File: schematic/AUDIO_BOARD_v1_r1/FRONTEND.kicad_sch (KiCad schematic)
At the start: 18 parts, among them J2 U.FL L in, J3 U.FL R in, U2 OPA1678, U3 OPA1678

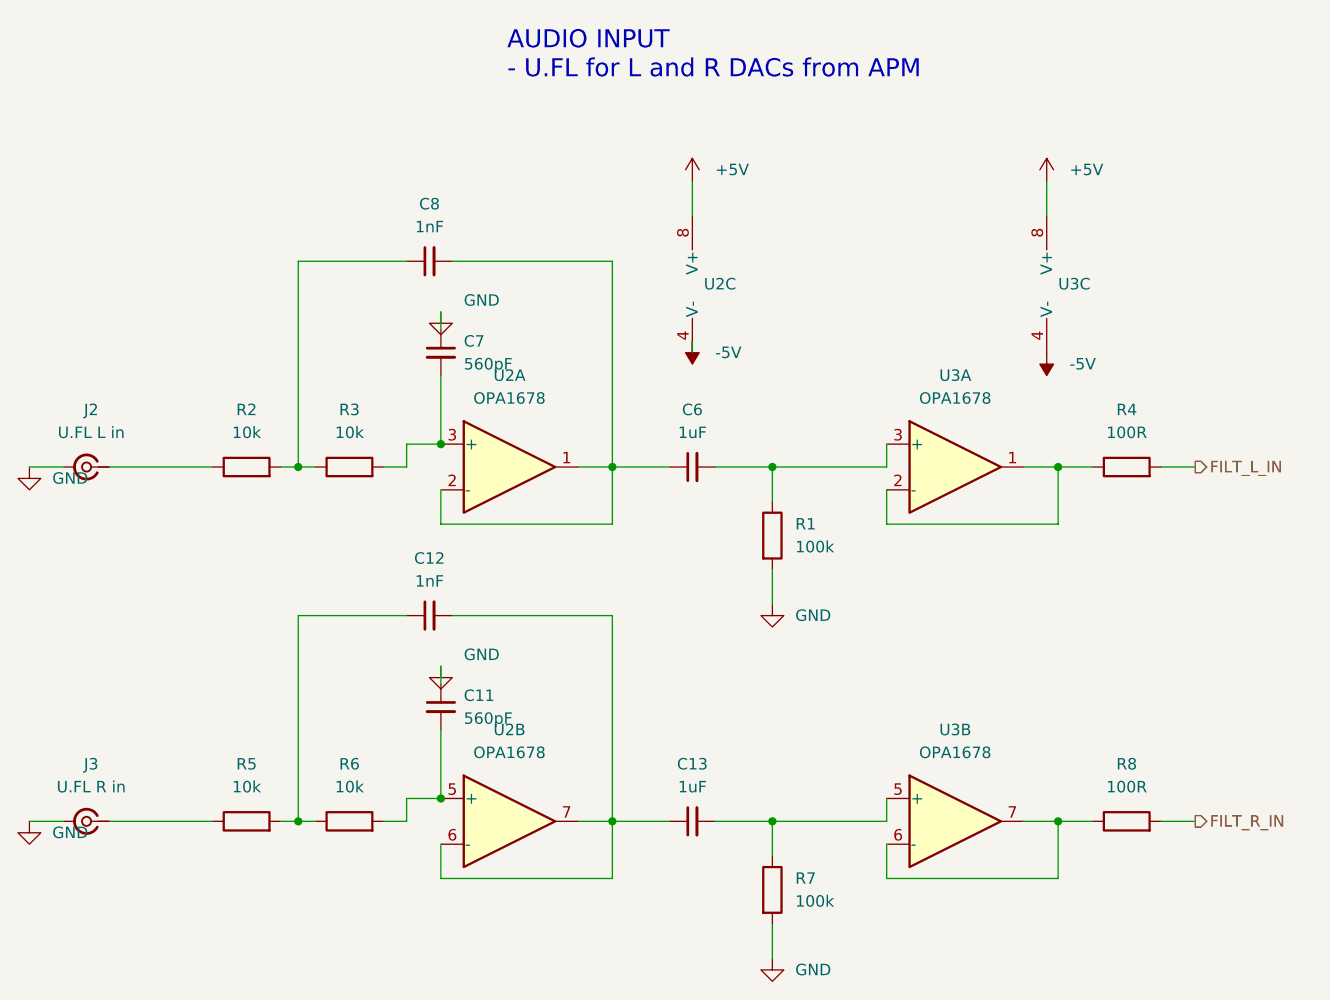
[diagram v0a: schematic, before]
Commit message: more placement and routing
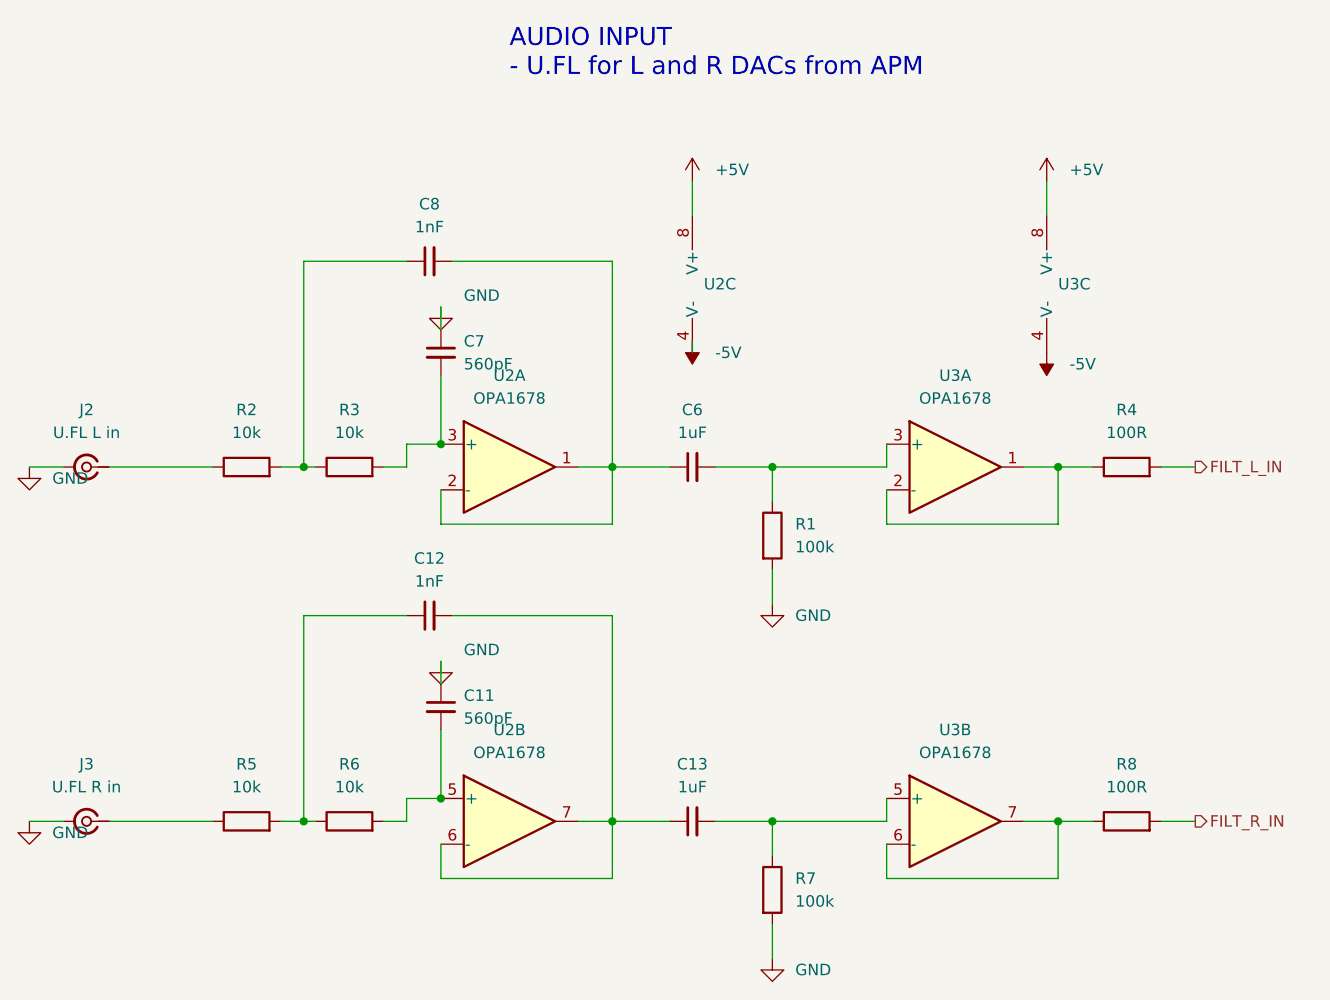
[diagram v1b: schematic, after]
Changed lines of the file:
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@@
 	(text "AUDIO INPUT\n- U.FL for L and R DACs from APM"
 		(exclude_from_sim no)
-		(at 77.216 85.344 0)
+		(at 77.47 85.09 0)
 		(effects
 			(font
@@
 	)
 	(junction
-		(at 54 128.27)
+		(at 54.61 128.27)
 		(diameter 0)
 		(color 0 0 0 0)
@@
 	)
 	(junction
-		(at 54 167.64)
+		(at 54.61 167.64)
 		(diameter 0)
 		(color 0 0 0 0)
@@
 	(wire
 		(pts
-			(xy 54 105.41) (xy 54 128.27)
+			(xy 54.61 105.41) (xy 54.61 128.27)
 		)
 		(stroke
@@
 	(wire
 		(pts
-			(xy 66.04 105.41) (xy 54 105.41)
+			(xy 66.04 105.41) (xy 54.61 105.41)
 		)
 		(stroke
@@
 	(wire
 		(pts
-			(xy 69.85 113.03) (xy 69.85 111.03)
+			(xy 69.85 113.03) (xy 69.85 110.49)
 		)
 		(stroke
@@
 	(wire
 		(pts
-			(xy 69.85 152.4) (xy 69.85 150.4)
+			(xy 69.85 152.4) (xy 69.85 149.86)
 		)
 		(stroke
@@
 	(wire
 		(pts
-			(xy 54 144.78) (xy 54 167.64)
+			(xy 54.61 144.78) (xy 54.61 167.64)
 		)
 		(stroke
@@
 	(wire
 		(pts
-			(xy 66.04 144.78) (xy 54 144.78)
+			(xy 66.04 144.78) (xy 54.61 144.78)
 		)
 		(stroke
@@
 		(fields_autoplaced yes)
 		(property "Reference" "C11"
-			(at 72.39 153.6762 0)
+			(at 72.39 153.67 0)
 			(show_name no)
 			(do_not_autoplace no)
@@
 		)
 		(property "Value" "560pF"
-			(at 72.39 156.2162 0)
+			(at 72.39 156.21 0)
 			(show_name no)
 			(do_not_autoplace no)
@@
 		(fields_autoplaced yes)
 		(property "Reference" "R7"
-			(at 109.22 173.9899 0)
+			(at 109.22 173.99 0)
 			(show_name no)
 			(do_not_autoplace no)
@@
 		)
 		(property "Value" "100k"
-			(at 109.22 176.5299 0)
+			(at 109.22 176.53 0)
 			(show_name no)
 			(do_not_autoplace no)
@@
 		(fields_autoplaced yes)
 		(property "Reference" "#PWR4012"
-			(at 24.13 170.64 0)
+			(at 24.13 170.18 0)
 			(hide yes)
 			(show_name no)
@@
 		)
 		(property "Value" "GND"
-			(at 26.67 168.9099 0)
+			(at 26.67 168.91 0)
 			(show_name no)
 			(do_not_autoplace no)
@@
 		(fields_autoplaced yes)
 		(property "Reference" "J3"
-			(at 30.9995 161.29 0)
+			(at 30.48 161.29 0)
 			(show_name no)
 			(do_not_autoplace no)
@@
 		)
 		(property "Value" "U.FL R in"
-			(at 30.9995 163.83 0)
+			(at 30.48 163.83 0)
 			(show_name no)
 			(do_not_autoplace no)
@@
 		(fields_autoplaced yes)
 		(property "Reference" "#PWR4018"
-			(at 137.16 99.52 0)
+			(at 137.16 99.06 0)
 			(hide yes)
 			(show_name no)
@@
 		)
 		(property "Value" "+5V"
-			(at 139.7 95.2499 0)
+			(at 139.7 95.25 0)
 			(show_name no)
 			(do_not_autoplace no)
@@
 		(fields_autoplaced yes)
 		(property "Reference" "C8"
-			(at 68.5863 99.06 90)
+			(at 68.58 99.06 90)
 			(show_name no)
 			(do_not_autoplace no)
@@
 		)
 		(property "Value" "1nF"
-			(at 68.5863 101.6 90)
+			(at 68.58 101.6 90)
 			(show_name no)
 			(do_not_autoplace no)
@@
 		(fields_autoplaced yes)
 		(property "Reference" "#PWR4019"
-			(at 97.79 99.52 0)
+			(at 97.79 99.06 0)
 			(hide yes)
 			(show_name no)
@@
 		)
 		(property "Value" "+5V"
-			(at 100.33 95.2499 0)
+			(at 100.33 95.25 0)
 			(show_name no)
 			(do_not_autoplace no)
@@
 		(fields_autoplaced yes)
 		(property "Reference" "#PWR4020"
-			(at 97.79 111.3 0)
+			(at 97.79 111.76 0)
 			(hide yes)
 			(show_name no)
@@
 		)
 		(property "Value" "-5V"
-			(at 100.33 115.5699 0)
+			(at 100.33 115.57 0)
 			(show_name no)
 			(do_not_autoplace no)
@@
 		(fields_autoplaced yes)
 		(property "Reference" "R1"
-			(at 109.22 134.6199 0)
+			(at 109.22 134.62 0)
 			(show_name no)
 			(do_not_autoplace no)
@@
 		)
 		(property "Value" "100k"
-			(at 109.22 137.1599 0)
+			(at 109.22 137.16 0)
 			(show_name no)
 			(do_not_autoplace no)
@@
 		(fields_autoplaced yes)
 		(property "Reference" "#PWR4024"
-			(at 24.13 131.27 0)
+			(at 24.13 130.81 0)
 			(hide yes)
 			(show_name no)
@@
 		)
 		(property "Value" "GND"
-			(at 26.67 129.5399 0)
+			(at 26.67 129.54 0)
 			(show_name no)
 			(do_not_autoplace no)
@@
 		(fields_autoplaced yes)
 		(property "Reference" "C6"
-			(at 97.7963 121.92 90)
+			(at 97.79 121.92 90)
 			(show_name no)
 			(do_not_autoplace no)
@@
 		)
 		(property "Value" "1uF"
-			(at 97.7963 124.46 90)
+			(at 97.79 124.46 90)
 			(show_name no)
 			(do_not_autoplace no)
@@
 		(fields_autoplaced yes)
 		(property "Reference" "C13"
-			(at 97.7963 161.29 90)
+			(at 97.79 161.29 90)
 			(show_name no)
 			(do_not_autoplace no)
@@
 		)
 		(property "Value" "1uF"
-			(at 97.7963 163.83 90)
+			(at 97.79 163.83 90)
 			(show_name no)
 			(do_not_autoplace no)
@@
 		(fields_autoplaced yes)
 		(property "Reference" "U2"
-			(at 99.06 107.9499 0)
+			(at 99.06 107.95 0)
 			(show_name no)
 			(do_not_autoplace no)
@@
 		)
 		(property "Value" "OPA1678"
-			(at 102.33 109.95 0)
+			(at 102.87 110.49 0)
 			(hide yes)
 			(show_name no)
@@
 		(fields_autoplaced yes)
 		(property "Reference" "#PWR4027"
-			(at 106.68 185.88 0)
+			(at 106.68 185.42 0)
 			(hide yes)
 			(show_name no)
@@
 		)
 		(property "Value" "GND"
-			(at 109.22 184.1499 0)
+			(at 109.22 184.15 0)
 			(show_name no)
 			(do_not_autoplace no)
@@
 		(fields_autoplaced yes)
 		(property "Reference" "#PWR4028"
-			(at 137.16 112.57 0)
+			(at 137.16 113.03 0)
 			(hide yes)
 			(show_name no)
@@
 		)
 		(property "Value" "-5V"
-			(at 139.7 116.8399 0)
+			(at 139.7 116.84 0)
 			(show_name no)
 			(do_not_autoplace no)
@@
 		(fields_autoplaced yes)
 		(property "Reference" "C12"
-			(at 68.5863 138.43 90)
+			(at 68.58 138.43 90)
 			(show_name no)
 			(do_not_autoplace no)
@@
 		)
 		(property "Value" "1nF"
-			(at 68.5863 140.97 90)
+			(at 68.58 140.97 90)
 			(show_name no)
 			(do_not_autoplace no)
@@
 		(fields_autoplaced yes)
 		(property "Reference" "C7"
-			(at 72.39 114.3062 0)
+			(at 72.39 114.3 0)
 			(show_name no)
 			(do_not_autoplace no)
@@
 		)
 		(property "Value" "560pF"
-			(at 72.39 116.8462 0)
+			(at 72.39 116.84 0)
 			(show_name no)
 			(do_not_autoplace no)
@@
 	(symbol
 		(lib_id "power:GND")
-		(at 69.85 111.03 0)
+		(at 69.85 110.49 0)
 		(unit 1)
 		(body_style 1)
@@
 		(fields_autoplaced yes)
 		(property "Reference" "#PWR4044"
-			(at 69.85 114.03 0)
+			(at 69.85 114.3 0)
 			(hide yes)
 			(show_name no)
@@
 		)
 		(property "Value" "GND"
-			(at 72.39 109.7599 0)
+			(at 72.39 109.22 0)
 			(show_name no)
 			(do_not_autoplace no)
@@
 		)
 		(property "Footprint" ""
-			(at 69.85 111.03 0)
+			(at 69.85 110.49 0)
 			(show_name no)
 			(do_not_autoplace no)
@@
 		)
 		(property "Datasheet" ""
-			(at 69.85 111.03 0)
+			(at 69.85 110.49 0)
 			(show_name no)
 			(do_not_autoplace no)
@@
 		)
 		(property "Description" ""
-			(at 69.85 111.03 0)
+			(at 69.85 110.49 0)
 			(show_name no)
 			(do_not_autoplace no)
@@
 	(symbol
 		(lib_id "power:GND")
-		(at 69.85 150.4 0)
+		(at 69.85 149.86 0)
 		(unit 1)
 		(body_style 1)
@@
 		(fields_autoplaced yes)
 		(property "Reference" "#PWR4045"
-			(at 69.85 153.4 0)
+			(at 69.85 153.67 0)
 			(hide yes)
 			(show_name no)
@@
 		)
 		(property "Value" "GND"
-			(at 72.39 149.1299 0)
+			(at 72.39 148.59 0)
 			(show_name no)
 			(do_not_autoplace no)
@@
 		)
 		(property "Footprint" ""
-			(at 69.85 150.4 0)
+			(at 69.85 149.86 0)
 			(show_name no)
 			(do_not_autoplace no)
@@
 		)
 		(property "Datasheet" ""
-			(at 69.85 150.4 0)
+			(at 69.85 149.86 0)
 			(show_name no)
 			(do_not_autoplace no)
@@
 		)
 		(property "Description" ""
-			(at 69.85 150.4 0)
+			(at 69.85 149.86 0)
 			(show_name no)
 			(do_not_autoplace no)
@@
 		(fields_autoplaced yes)
 		(property "Reference" "#PWR4046"
-			(at 106.68 146.51 0)
+			(at 106.68 146.05 0)
 			(hide yes)
 			(show_name no)
@@
 		)
 		(property "Value" "GND"
-			(at 109.22 144.7799 0)
+			(at 109.22 144.78 0)
 			(show_name no)
 			(do_not_autoplace no)
@@
 		(fields_autoplaced yes)
 		(property "Reference" "U3"
-			(at 138.43 107.9499 0)
+			(at 138.43 107.95 0)
 			(show_name no)
 			(do_not_autoplace no)
@@
 		)
 		(property "Value" "OPA1678"
-			(at 141.7 109.95 0)
+			(at 142.24 110.49 0)
 			(hide yes)
 			(show_name no)
@@
 		(fields_autoplaced yes)
 		(property "Reference" "J2"
-			(at 30.9995 121.92 0)
+			(at 30.48 121.92 0)
 			(show_name no)
 			(do_not_autoplace no)
@@
 		)
 		(property "Value" "U.FL L in"
-			(at 30.9995 124.46 0)
+			(at 30.48 124.46 0)
 			(show_name no)
 			(do_not_autoplace no)

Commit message: U2B not connected
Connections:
- net at C11.2, R6.2: no longer U2.5 (+)
- net at C12.2, C13.1: no longer U2.6 (-), U2.7
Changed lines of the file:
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@@
-	)
-	(junction
-		(at 69.85 165.1)
-		(diameter 0)
-		(color 0 0 0 0)
 	)
 	(junction
@@
 		(lib_id "Amplifier_Operational:OPA1678")
 		(at 77.47 167.64 0)
+		(mirror y)
 		(unit 2)
 		(body_style 1)
@@
 		(in_pos_files yes)
 		(dnp no)
-		(fields_autoplaced yes)
 		(property "Reference" "U2"
 			(at 77.47 157.48 0)

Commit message: more routing. more placement
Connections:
- net at C11.2, R6.2: now also U2.5 (+)
- net at U2.6 (-): now also C12.2, C13.1, U2.7
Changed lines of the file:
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@@
 		(lib_id "Amplifier_Operational:OPA1678")
 		(at 77.47 167.64 0)
-		(mirror y)
 		(unit 2)
 		(body_style 1)

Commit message: try autorouter?
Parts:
- U2, U3: footprint Package_DIP:DIP-8_W7.62mm_SMDSocket_SmallPads -> Package_SO:SOIC-8_3.9x4.9mm_P1.27mm
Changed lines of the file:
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@@
 			)
 		)
-		(property "Footprint" "Package_DIP:DIP-8_W7.62mm_SMDSocket_SmallPads"
+		(property "Footprint" "Package_SO:SOIC-8_3.9x4.9mm_P1.27mm"
 			(at 77.47 167.64 0)
 			(hide yes)
@@
 			)
 		)
-		(property "Footprint" "Package_DIP:DIP-8_W7.62mm_SMDSocket_SmallPads"
+		(property "Footprint" "Package_SO:SOIC-8_3.9x4.9mm_P1.27mm"
 			(at 127 167.64 0)
 			(hide yes)
@@
 			)
 		)
-		(property "Footprint" "Package_DIP:DIP-8_W7.62mm_SMDSocket_SmallPads"
+		(property "Footprint" "Package_SO:SOIC-8_3.9x4.9mm_P1.27mm"
 			(at 77.47 128.27 0)
 			(hide yes)
@@
 			)
 		)
-		(property "Footprint" "Package_DIP:DIP-8_W7.62mm_SMDSocket_SmallPads"
+		(property "Footprint" "Package_SO:SOIC-8_3.9x4.9mm_P1.27mm"
 			(at 127 128.27 0)
 			(hide yes)
